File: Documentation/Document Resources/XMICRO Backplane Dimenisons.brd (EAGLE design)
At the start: 203.2 x 70.6 mm, 4 parts

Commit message: Updated specification document and dimensional drawings
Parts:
- added 4: XMICRO-BUS-PHYSICAL-EDGE62F, Custom:EDGE62F
- moved 0 25.5 mm to (152.4, 100.3)
- moved 1 25.5 mm to (152.4, 81.3)
- moved 2 25.5 mm to (152.4, 62.2)
- moved 3 25.5 mm to (152.4, 43.2)
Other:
- board text added: "Notes: 1. All dimensions are in inches. 2. Slot connectors must be oriented as shown. 3. Pin 1 must be marked on at least one slot. 4. Each slot number must be indicated on the PCB. 5. All backplane slots must fit full-dimension cards 6. Slots at either end of the backplane must allow a minimim 0.1" clearance between full dimension cards and chassis. 7. Maximum component height under cards may no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"
- board text removed: "Notes: 1. Slot connectors must be oriented as shown. 2. Pin 1 must be marked on at least one slot. 3. Each slot number must be indicated on the PCB. 4. All backplane slots must fit full-dimension cards 5. Slots at either end of the backplane must allow a minimim 0.1" clearance between full dimension cards and chassis. 6. Maximum component height under cards may not exceed the edge connectors."
- board text removed: "V1.0 2018-10-07"
- board text removed: "XMICRO BACKPLANE DIMENSIONS"

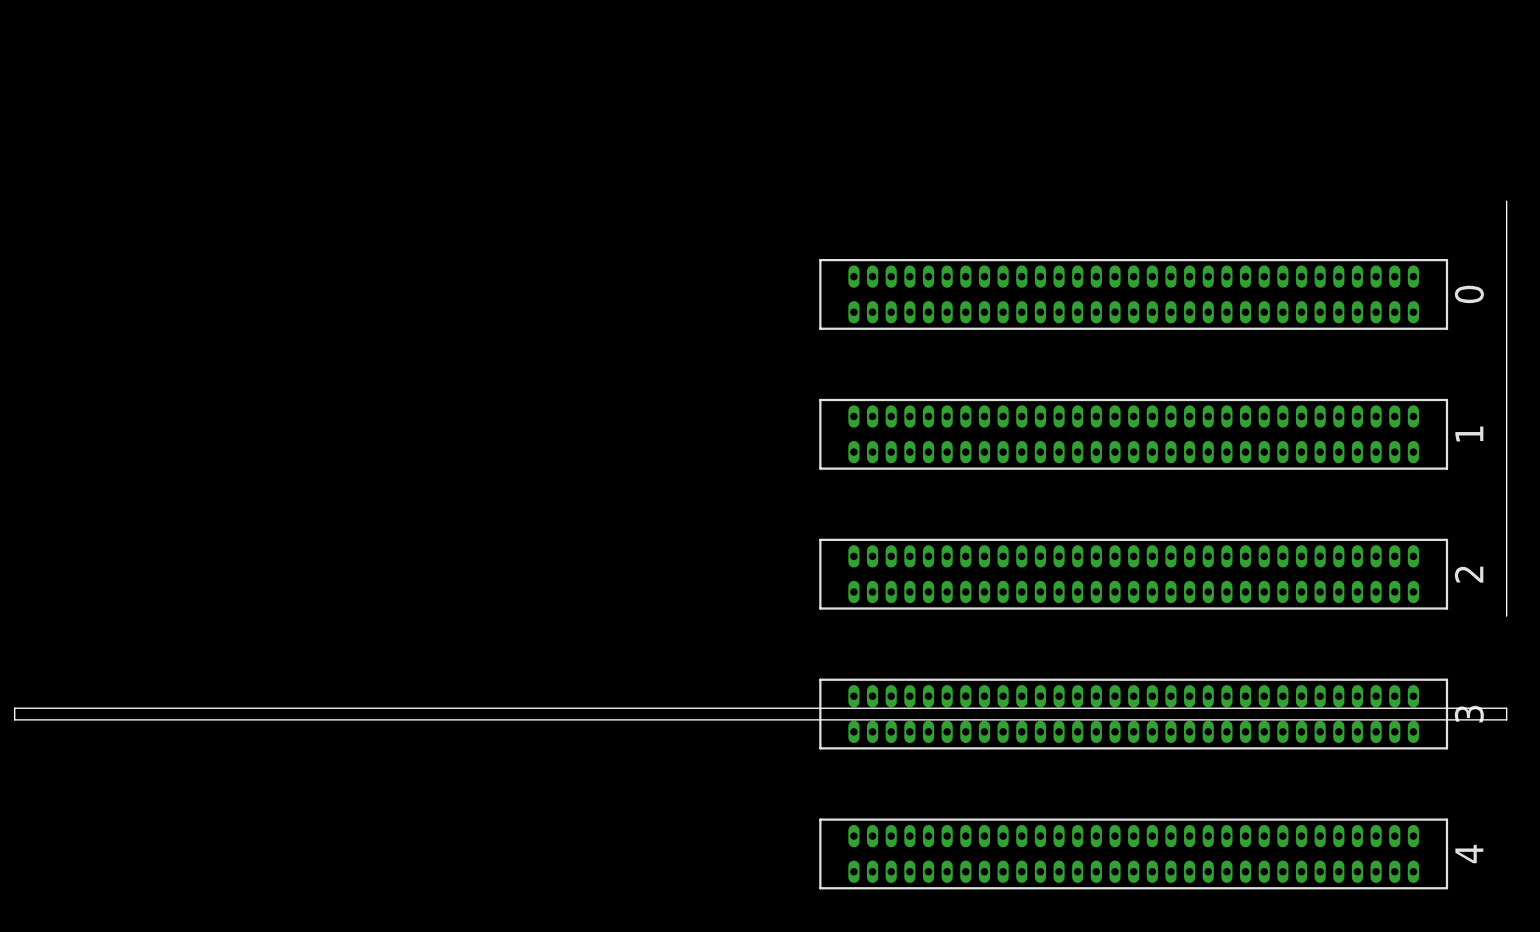
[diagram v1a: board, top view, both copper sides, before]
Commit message: Updated physical dimensions (PCB rear edge to chassis)
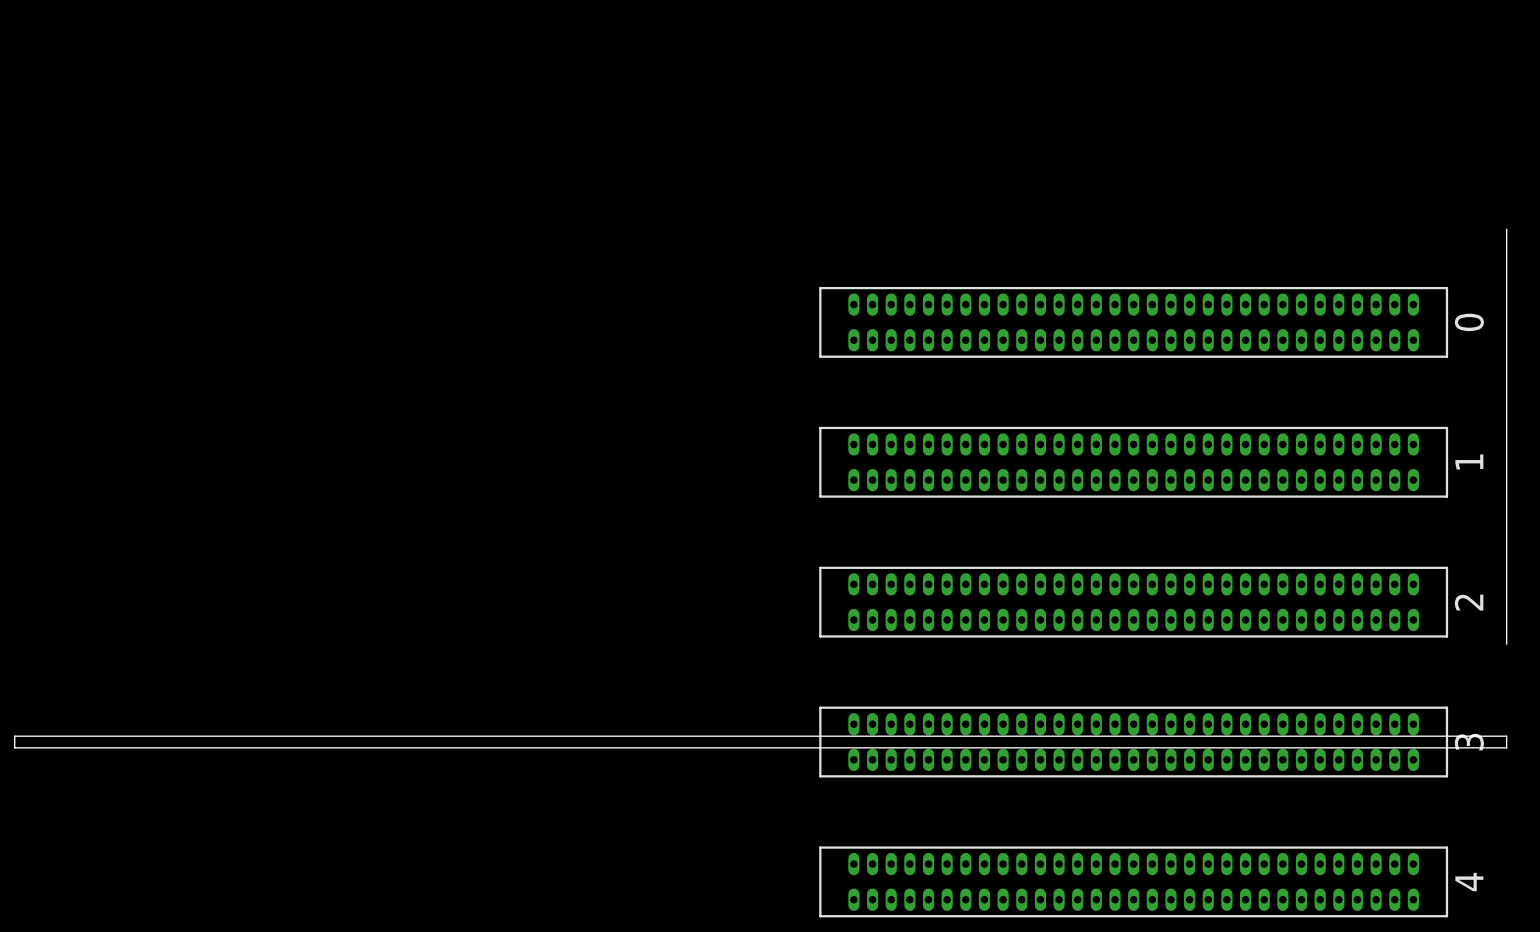
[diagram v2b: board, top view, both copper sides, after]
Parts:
- moved 0 3.81 mm to (152.4, 96.5)
- moved 1 3.81 mm to (152.4, 77.5)
- moved 3 3.81 mm to (152.4, 39.4)
- moved 4 3.81 mm to (152.4, 20.3)
- moved 2 3.81 mm to (152.4, 58.4)
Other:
- board text added: "INSIDE SURFACE OF CHASSIS"
- board text added: "Notes: 1. All dimensions are in inches. 2. Slot connectors must be oriented as shown. 3. Pin 1 must be marked on at least one slot. 4. Each slot number must be indicated on the PCB. 5. All backplane slots must fit full-dimension cards. 6. Maximum component height under cards may not exceed the edge connectors."
- board text removed: "Notes: 1. All dimensions are in inches. 2. Slot connectors must be oriented as shown. 3. Pin 1 must be marked on at least one slot. 4. Each slot number must be indicated on the PCB. 5. All backplane slots must fit full-dimension cards 6. Slots at either end of the backplane must allow a minimim 0.1" clearance between full dimension cards and chassis. 7. Maximum component height under cards may no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"
- board text removed: "OUTSIDE SURFACE OF CHASSIS"
